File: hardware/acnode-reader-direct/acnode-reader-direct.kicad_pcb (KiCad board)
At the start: 2 copper layers, 53 x 72.1 mm, 10 parts, among them J1 RJ45, J2_RGB_LED R- +5V G- B-, J3 BUTTON N/O, J4 Elechouse_V4_Conn

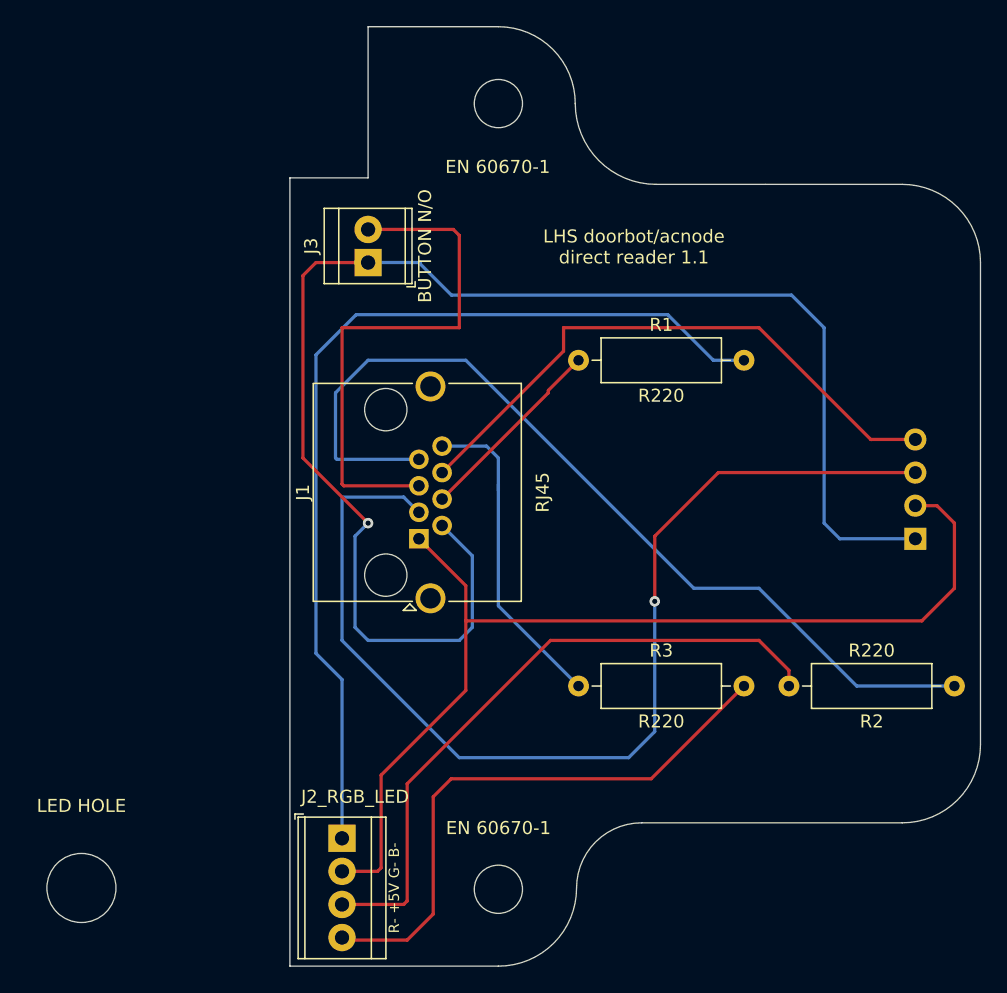
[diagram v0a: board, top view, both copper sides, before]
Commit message: update with optional +5V output for button
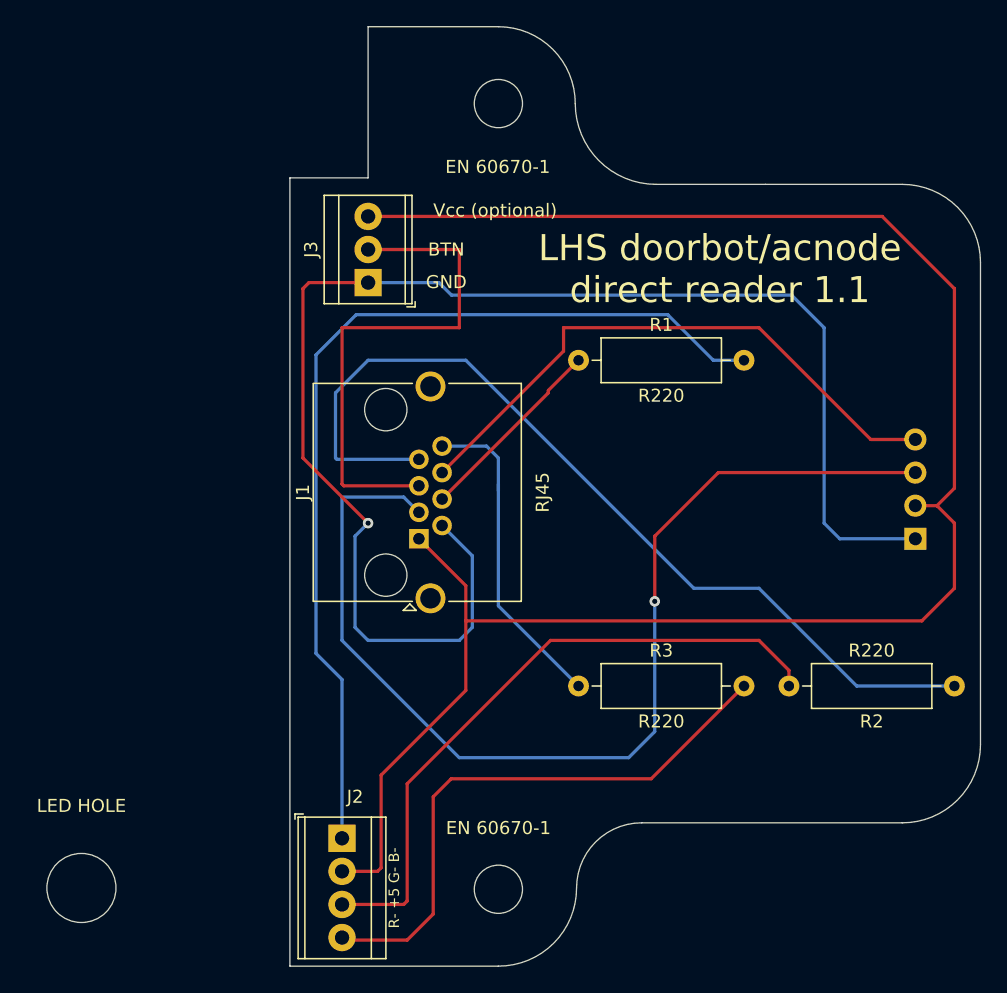
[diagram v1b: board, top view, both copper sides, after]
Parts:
- J2: renamed from J2_RGB_LED; value R- +5V G- B- -> R- +5 G- B-
- J3: footprint TerminalBlock_TE-Connectivity:TerminalBlock_TE_282834-2_1x02_P2.54mm_Horizontal -> TerminalBlock_TE-Connectivity:TerminalBlock_TE_282834-3_1x03_P2.54mm_Horizontal
- J4: value Elechouse_V4_Conn -> Conn_01x04
- moved J3 1.54 mm to (85.0, 56.5)
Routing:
- net /+5V_Vcc: track 79.6 -> 144.1 mm
- net /GND: track 113.2 -> 111.2 mm
- net /BTN: track 41.2 -> 40.0 mm
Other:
- board text added: "+5V Vcc"
- board text added: "BTN"
- board text added: "GND"
- board text added: "PN532 RXD"
- board text added: "PN532 TXD"
- board text added: "Vcc (optional)"

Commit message: rev 1.1a, including build photo of rev 1.1
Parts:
- removed LED HOLE: MountingHole_5.3mm_M5, MountingHole:MountingHole_5.3mm_M5
- J2: value R- +5 G- B- -> B- G- +5 R-
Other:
- board text added: "LHS doorbot/acnode direct reader 1.1a"
- board text removed: "LHS doorbot/acnode direct reader 1.1"
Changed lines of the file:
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@@
       (layerselection 0x00010fc_ffffffff)
       (disableapertmacros false)
-      (usegerberextensions false)
+      (usegerberextensions true)
       (usegerberattributes true)
       (usegerberadvancedattributes true)
-      (creategerberjobfile true)
+      (creategerberjobfile false)
       (svguseinch false)
       (svgprecision 6)
@@
       (plotinvisibletext false)
       (sketchpadsonfab false)
-      (subtractmaskfromsilk false)
+      (subtractmaskfromsilk true)
       (outputformat 1)
       (mirror false)
-      (drillshape 1)
+      (drillshape 0)
       (scaleselection 1)
-      (outputdirectory "")
+      (outputdirectory "gerbers/")
     )
   )
@@
       (effects (font (size 1 1) (thickness 0.15)))
     )
-    (fp_text value "R- +5 G- B-" (at 3.8105 -4 90) (layer "F.SilkS")
+    (fp_text value "B- G- +5 R-" (at 3.8105 -4 90) (layer "F.SilkS")
       (effects (font (size 0.8 0.8) (thickness 0.15)))
     )
@@
       (rotate (xyz 0 0 0))
     )
-  )
-  (footprint "MountingHole:MountingHole_5.3mm_M5" (layer "F.Cu")
-    (at 63 103)
-    (descr "Mounting Hole 5.3mm, no annular, M5")
-    (tags "mounting hole 5.3mm no annular m5")
-    (attr exclude_from_pos_files exclude_from_bom)
-    (fp_text reference "LED HOLE" (at 0 -6.3) (layer "F.SilkS")
-      (effects (font (size 1 1) (thickness 0.15)))
-    )
-    (fp_text value "MountingHole_5.3mm_M5" (at 0 6.3) (layer "F.Fab")
-      (effects (font (size 1 1) (thickness 0.15)))
-    )
-    (fp_text user "${REFERENCE}" (at 0.3 0) (layer "F.Fab")
-      (effects (font (size 1 1) (thickness 0.15)))
-    )
-    (fp_circle (center 0 0) (end 5.3 0) (layer "Cmts.User") (width 0.15) (fill none))
-    (fp_circle (center 0 0) (end 5.55 0) (layer "F.CrtYd") (width 0.05) (fill none))
-    (pad "" np_thru_hole circle locked (at 0 0) (size 5.3 5.3) (drill 5.3) (layers *.Cu *.Mask))
   )
   (footprint "Resistor_THT:R_Axial_DIN0309_L9.0mm_D3.2mm_P12.70mm_Horizontal" (layer "F.Cu")
@@
     (effects (font (size 1 1) (thickness 0.15)))
   )
-  (gr_text "LHS doorbot/acnode\ndirect reader 1.1" (at 112 55.5) (layer "F.SilkS")
+  (gr_text "LHS doorbot/acnode\ndirect reader 1.1a" (at 112 55.5) (layer "F.SilkS")
     (effects (font (size 2 2) (thickness 0.3)))
   )
